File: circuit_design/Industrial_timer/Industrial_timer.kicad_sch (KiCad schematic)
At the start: 31 parts, among them Q101 MMBT3904, Q103 DMP4065SQ, U101 SL78M05, U102 LM358_SIM

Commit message: Saving updated circuits.
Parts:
- removed C108: C, symbol Device:C
- removed R113: R_US, symbol Device:R_US

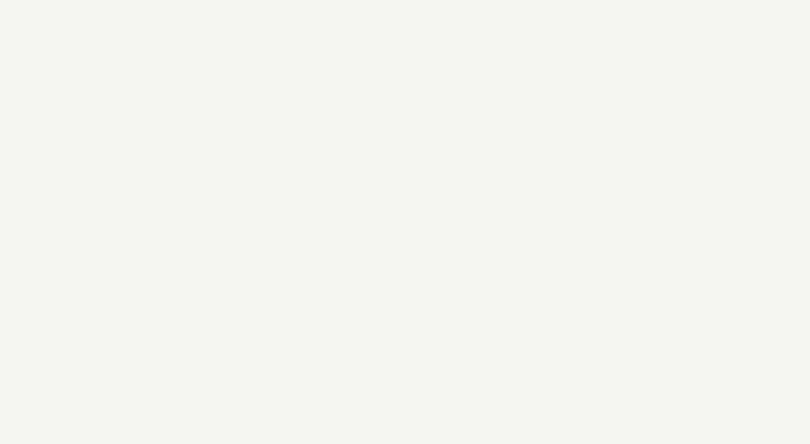
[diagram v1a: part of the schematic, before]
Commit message: Adding a generic RC circuit. To be removed later.
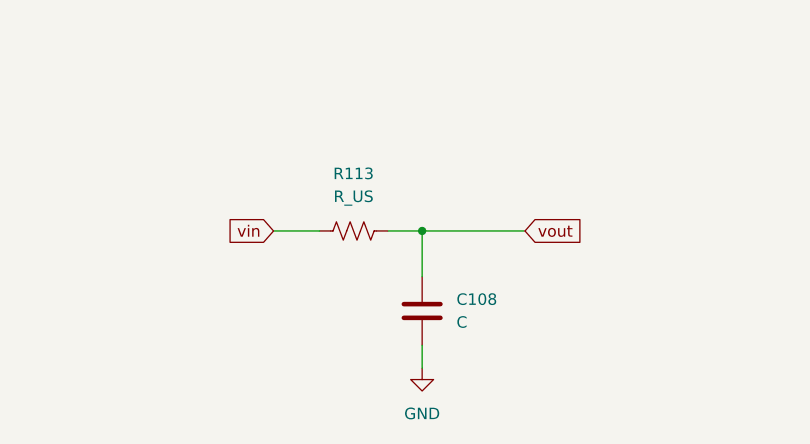
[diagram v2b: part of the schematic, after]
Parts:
- added C108: C, symbol Device:C
- added R113: R_US, symbol Device:R_US
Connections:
- net GND: now also C108.2
- new net vin: R113.1
- new net vout: C108.1, R113.2
